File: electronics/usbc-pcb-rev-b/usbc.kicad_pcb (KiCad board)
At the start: 2 copper layers, 19 x 16 mm, 8 parts, among them J1 USB4736-GF-A, J2 To control board

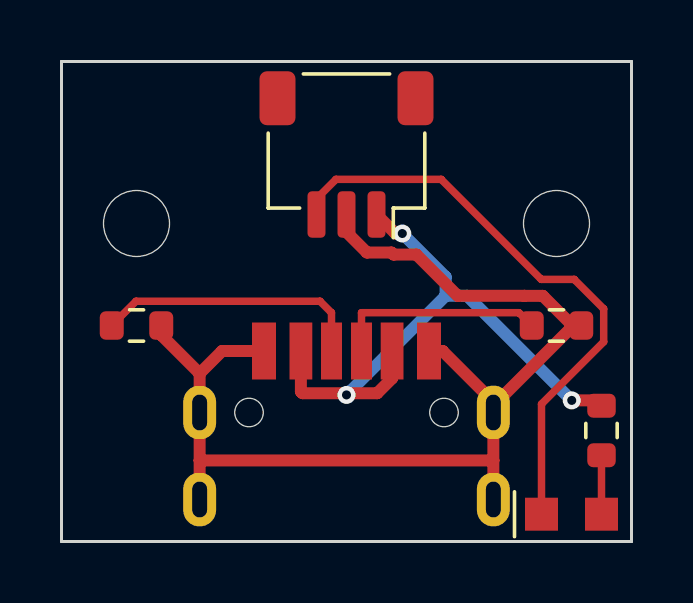
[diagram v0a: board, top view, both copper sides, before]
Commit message: Match the USB4736 footprint to GCT's layout
The signal pads sat 0.10 mm closer to the board edge than GCT's
recommended layout (drawing USB4736 rev. A). Every other feature
matched. The USB-C board rev B is regenerated; ERC and DRC show no
errors. Rev A has the same offset and is noted, not changed.

Signed-off-by: Marc Cirauqui <marc@tetrate.io>
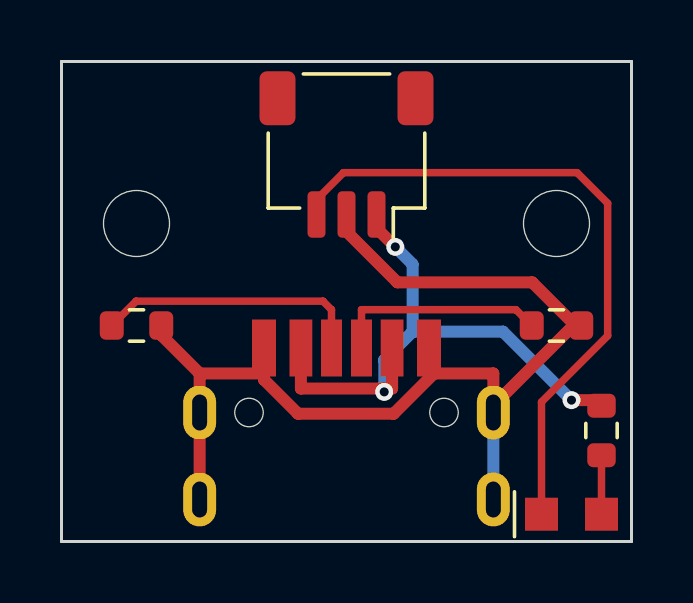
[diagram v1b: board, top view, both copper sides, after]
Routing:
- net /LED_K: track 19.9 -> 22.3 mm
- net GND: track 38.1 -> 36.8 mm
- net /VBUS: track 20.8 -> 20.0 mm
